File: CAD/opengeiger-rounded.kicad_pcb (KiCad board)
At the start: 2 copper layers, 116 x 31 mm, 91 parts, among them J1 Conn_01x04, J10 Conn_01x04, J3 Conn_01x06, J5 Conn_01x04, J8 USB_C_Receptacle_USB2.0, Q1 STN0214, Q2 PMBT2222A,215, Q3 DMG2302UK-7, Q4 UMH3N, SW1 TL3301NF160QG/TR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

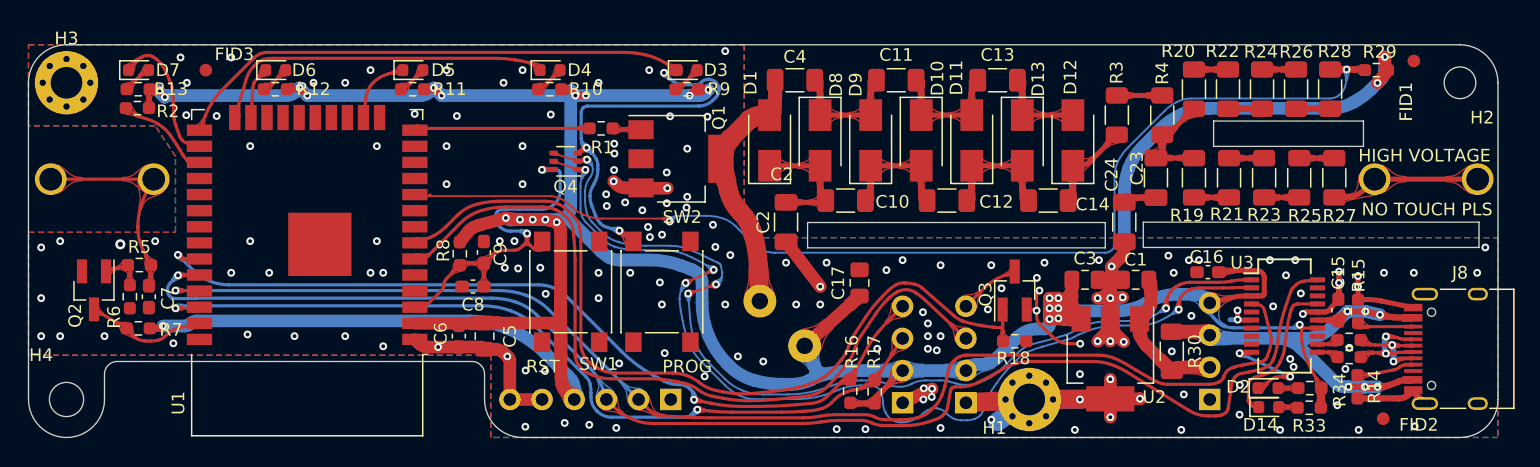
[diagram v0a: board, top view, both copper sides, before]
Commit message: Feat: Production files for JLC prod, readme update
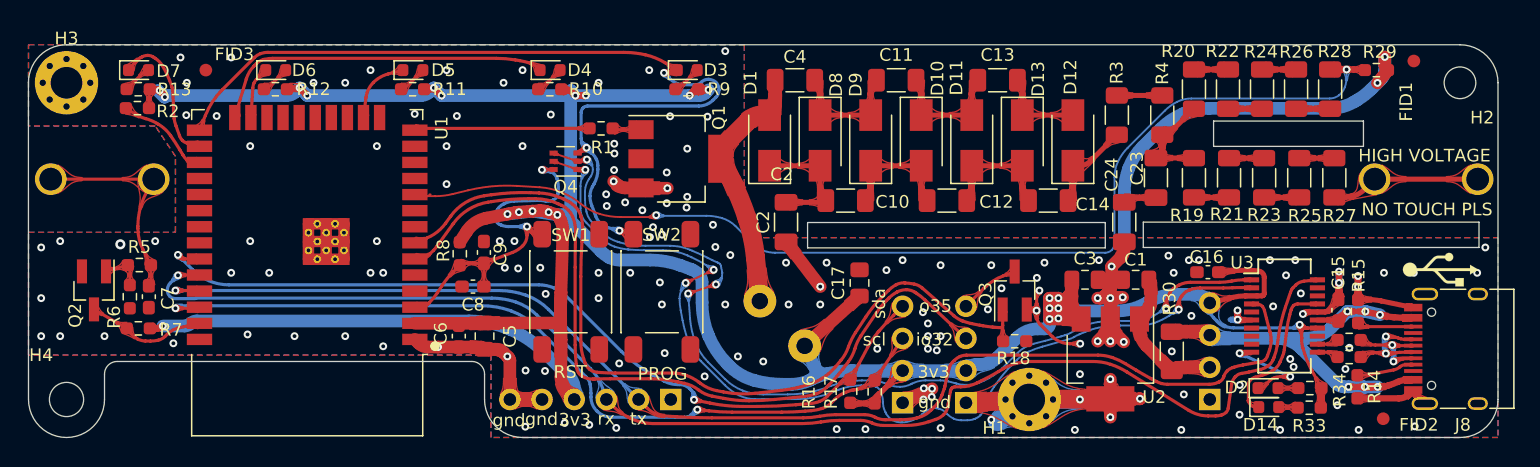
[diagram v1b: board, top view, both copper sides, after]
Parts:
- added G***: LOGO, LOGO, B.Cu at (166.5, 99.5)
- SW1, SW2: footprint Button_Switch_SMD:SW_SPST_PTS645 -> eikgeiger:SW_TL3301NF160QG_TR
- U1: footprint RF_Module:ESP32-WROOM-32 -> eikgeiger:ESP32-WROOM-32
- moved kibuzzard-637F3F6B 0.82 mm to (86.0, 96.5)
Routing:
- net GNDREF: track 132.5 -> 149.3 mm, vias 170 -> 169
- net +3.3V: track 274.3 -> 278.7 mm
- net RST: track 29.8 -> 27.6 mm
- net GPIO32: track 62.2 -> 63.7 mm
- net CLICKER: track 66.8 -> 68.3 mm
- net /SWITCH: track 20.8 -> 20.3 mm
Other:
- board text added: "3v3"
- board text added: "3v3_REG"
- board text added: "5v0_USB"
- board text added: "5v0_card"
- board text added: "GND"
- board text added: "gnd"
- board text added: "io32"
- board text added: "o35"
- board text added: "rx"
- board text added: "scl"
- board text added: "sda"
- board text added: "tx"

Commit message: Feat: New prod, working code
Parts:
- H4: footprint MountingHole:MountingHole_2.7mm -> MountingHole:MountingHole_2.5mm
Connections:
- U1 pad 6: GPIO32 -> unconnected-(U1-Pad6)
- U1 pad 7: CLICKER -> unconnected-(U1-Pad7)
- U1 pad 8: unconnected-(U1-Pad8) -> CLICKER
- U1 pad 9: unconnected-(U1-Pad9) -> GPIO32
- U3 pad 13: unconnected-(U3-Pad13) -> 3v3fdti
- U3 pad 14: +3.3V -> 3v3fdti
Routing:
- net +3.3V: track 278.7 -> 275.0 mm
- net 3v3fdti: track 0.00 -> 1.83 mm
- net GPIO32: track 63.7 -> 62.6 mm, vias 0 -> 2
- net CLICKER: track 68.3 -> 67.7 mm
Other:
- board text added: "V 0.2.1"
- board text removed: "C2"
- board text removed: "V 0.2.0"

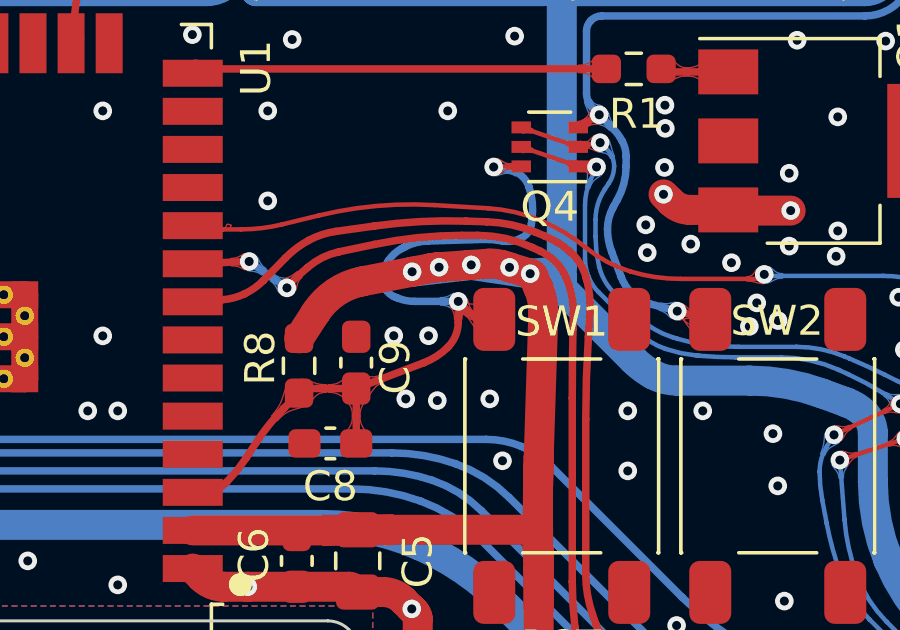
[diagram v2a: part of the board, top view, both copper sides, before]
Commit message: Feat: New order from jlcpcb rev 0.2.1
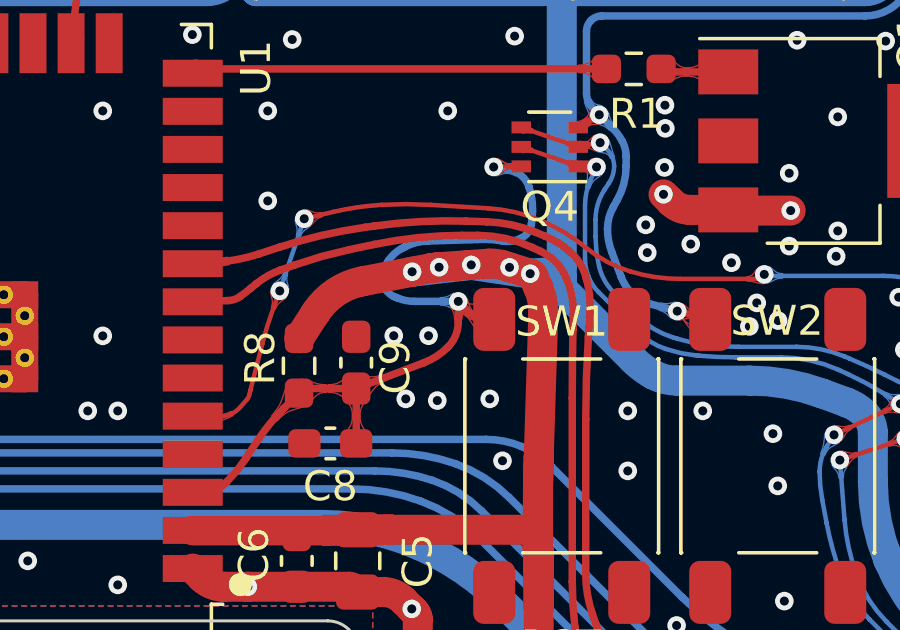
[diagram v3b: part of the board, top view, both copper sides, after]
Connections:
- U1 pad 10: RFB -> unconnected-(U1-Pad10)
- U1 pad 5: unconnected-(U1-Pad5) -> RFB
- U1 pad 8: CLICKER -> GPIO32
- U1 pad 9: GPIO32 -> CLICKER
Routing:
- net RFB: track 88.4 -> 92.9 mm, vias 2 -> 4
- net CLICKER: track 67.7 -> 67.1 mm
- net GPIO32: track 62.6 -> 62.3 mm, vias 2 -> 0
